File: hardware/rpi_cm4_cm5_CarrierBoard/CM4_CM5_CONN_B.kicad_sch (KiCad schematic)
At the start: 24 parts, among them U17 RPI_CMx_B

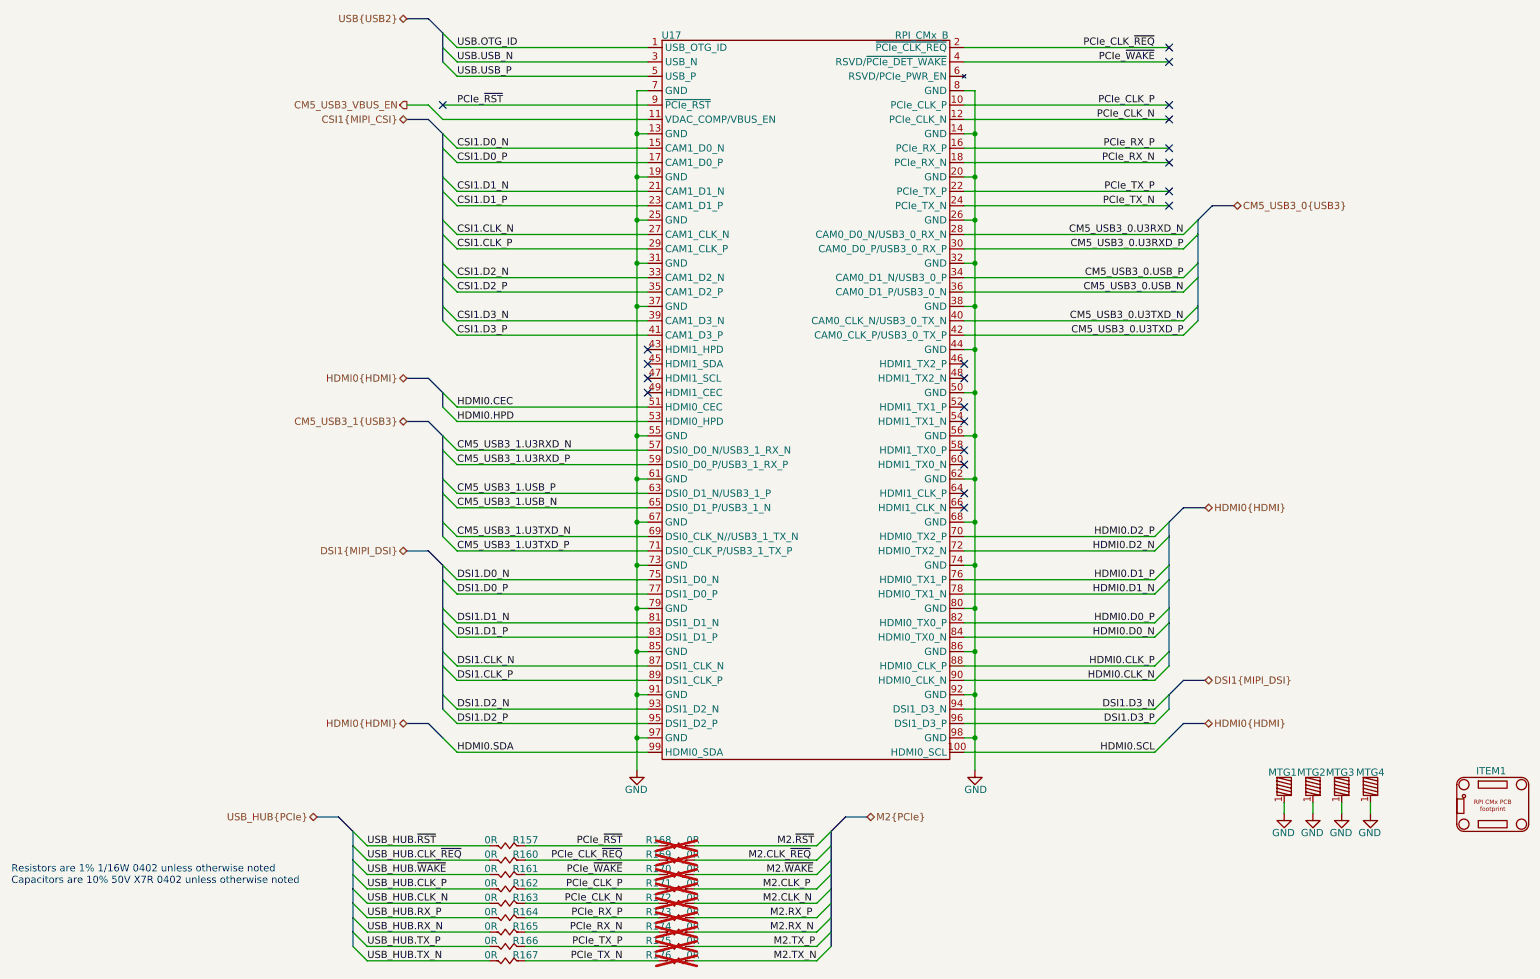
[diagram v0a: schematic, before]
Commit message: Add power-up and power kill sequences Modify schematics to add net classes for DiffPairs
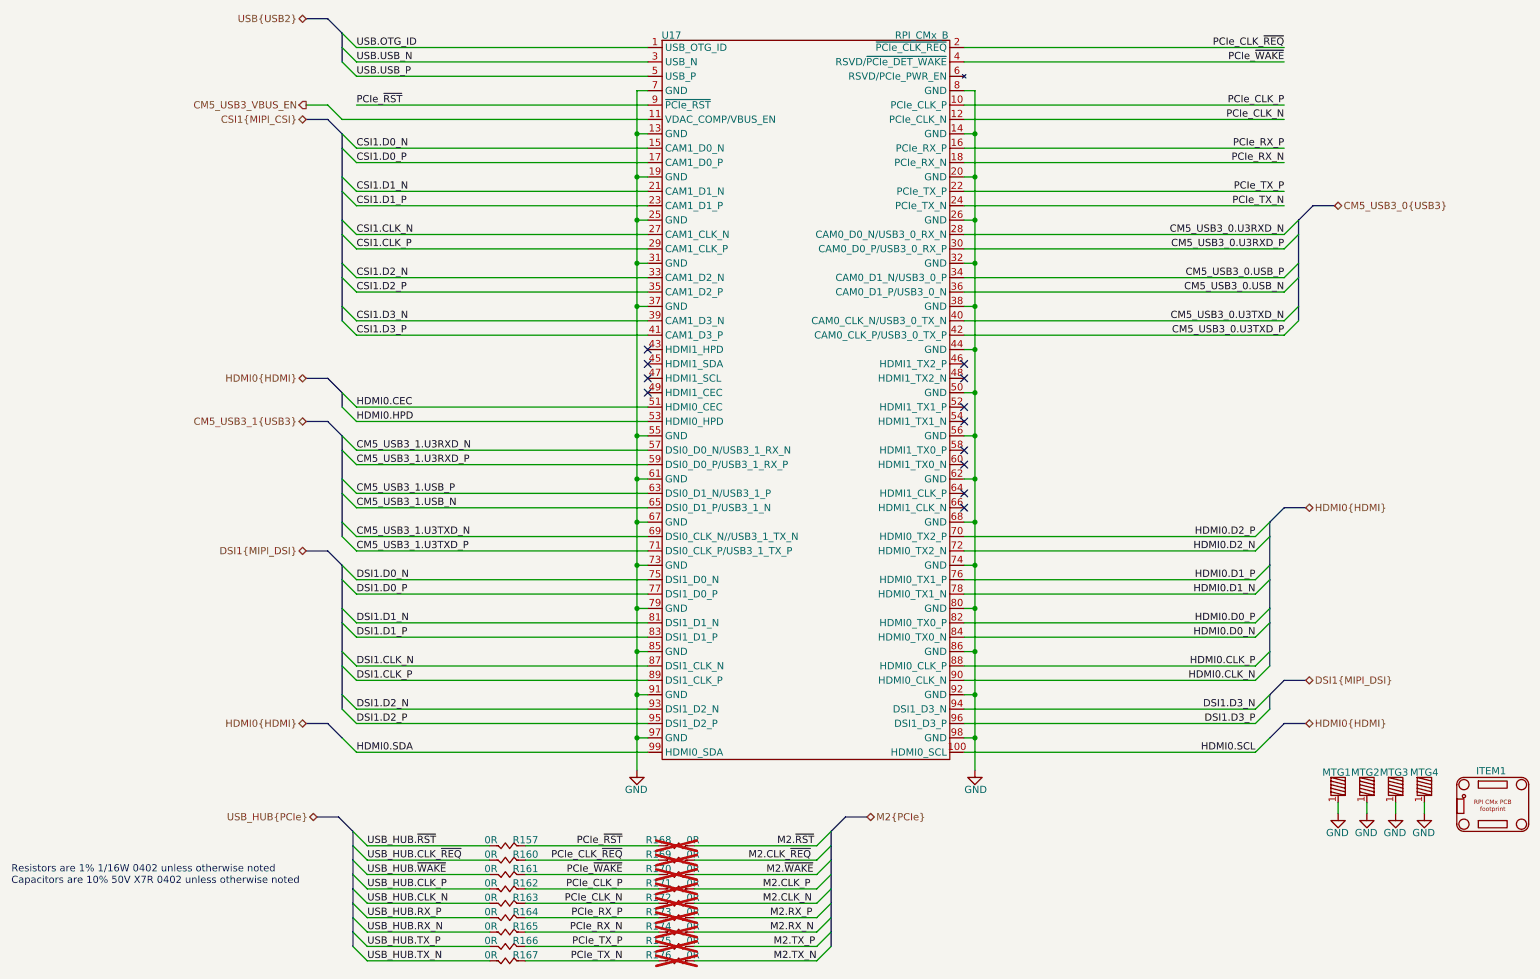
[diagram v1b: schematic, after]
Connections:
- no-connect marks 21 -> 12
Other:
- moved on the sheet: MTG1, MTG2, MTG3, MTG4

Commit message: Significant update to schematics Add codec, Mikrobus, PIC32A Add power table, design notes for pinmux Add datasheets
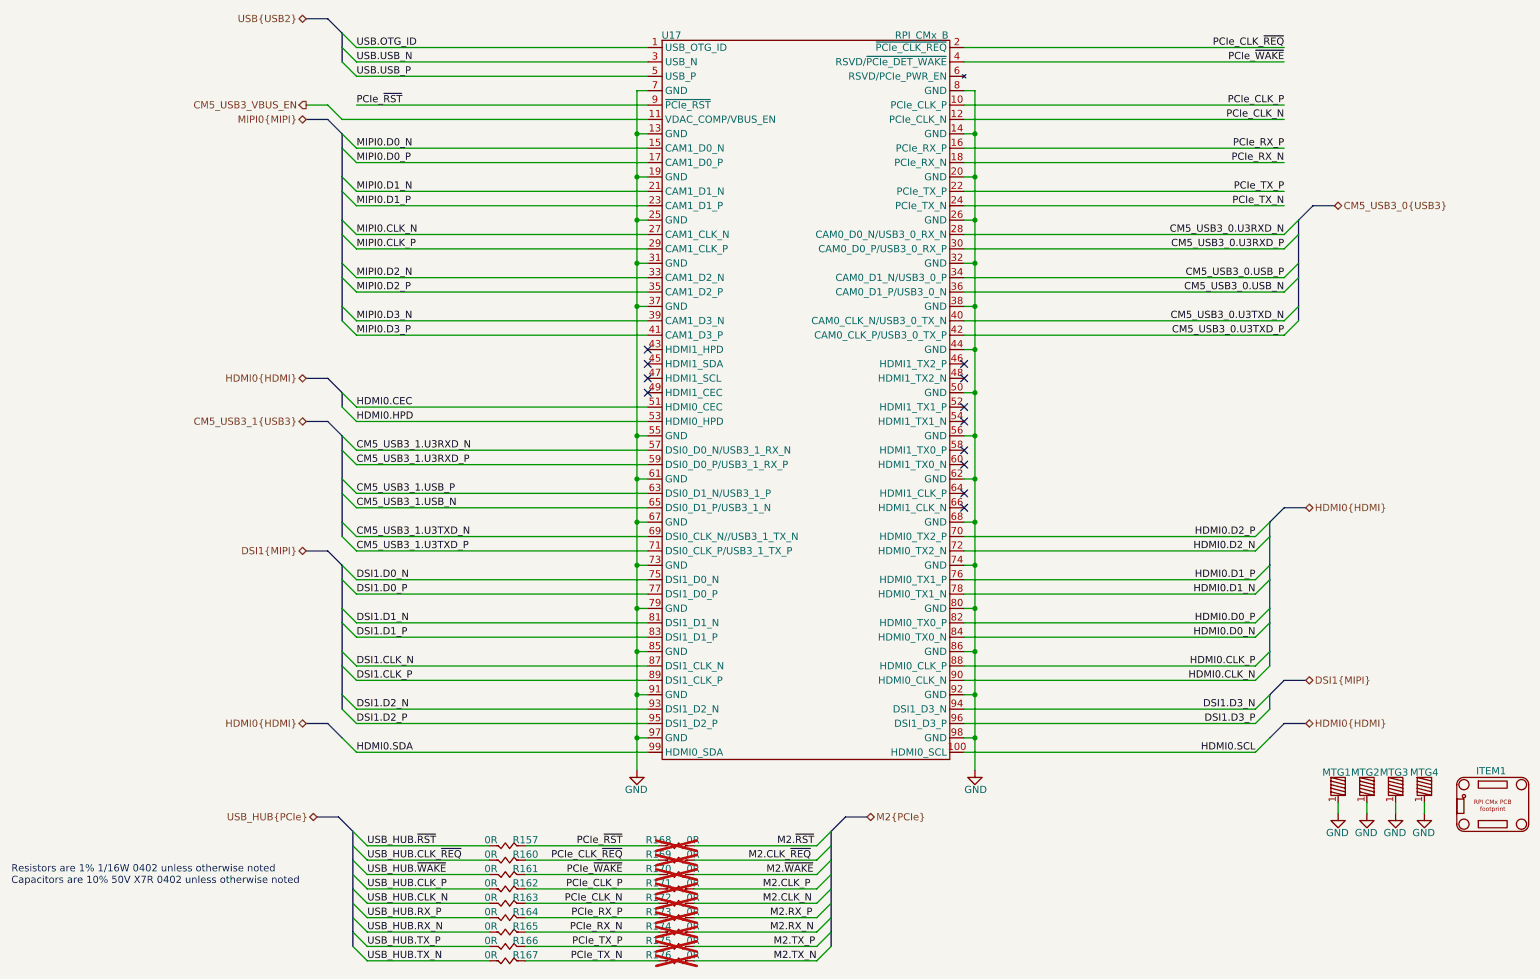
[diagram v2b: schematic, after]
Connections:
- net CSI1.CLK_N renamed MIPI0.CLK_N
- net CSI1.CLK_P renamed MIPI0.CLK_P
- net CSI1.D0_N renamed MIPI0.D0_N
- net CSI1.D0_P renamed MIPI0.D0_P
- net CSI1.D1_N renamed MIPI0.D1_N
- net CSI1.D1_P renamed MIPI0.D1_P
- net CSI1.D2_N renamed MIPI0.D2_N
- net CSI1.D2_P renamed MIPI0.D2_P
- net CSI1.D3_N renamed MIPI0.D3_N
- net CSI1.D3_P renamed MIPI0.D3_P
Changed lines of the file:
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@@
 		(comment 8 "WIP")
 	)
-	(bus_alias "MIPI_CSI"
-		(members "D0_P" "D0_N" "D1_P" "D1_N" "D2_P" "D2_N" "D3_P" "D3_N" "CLK_P"
-			"CLK_N"
-		)
-	)
 	(text "Resistors are 1% 1/16W 0402 unless otherwise noted\nCapacitors are 10% 50V X7R 0402 unless otherwise noted"
 		(exclude_from_sim no)
@@
 		)
 	)
-	(label "CSI1.D2_N"
+	(label "MIPI0.D2_N"
 		(at 73.66 65.405 0)
 		(effects
@@
 		)
 	)
-	(label "CSI1.D3_P"
+	(label "MIPI0.D3_P"
 		(at 73.66 75.565 0)
 		(effects
@@
 		)
 	)
-	(label "CSI1.D0_P"
+	(label "MIPI0.D0_P"
 		(at 73.66 45.085 0)
 		(effects
@@
 		)
 	)
-	(label "CSI1.D2_P"
+	(label "MIPI0.D2_P"
 		(at 73.66 67.945 0)
 		(effects
@@
 		)
 	)
-	(label "CSI1.CLK_N"
+	(label "MIPI0.CLK_N"
 		(at 73.66 57.785 0)
 		(effects
@@
 		)
 	)
-	(label "CSI1.D0_N"
+	(label "MIPI0.D0_N"
 		(at 73.66 42.545 0)
 		(effects
@@
 		)
 	)
-	(label "CSI1.D1_N"
+	(label "MIPI0.D1_N"
 		(at 73.66 50.165 0)
 		(effects
@@
 		)
 	)
-	(label "CSI1.CLK_P"
+	(label "MIPI0.CLK_P"
 		(at 73.66 60.325 0)
 		(effects
@@
 		)
 	)
-	(label "CSI1.D1_P"
+	(label "MIPI0.D1_P"
 		(at 73.66 52.705 0)
 		(effects
@@
 		)
 	)
-	(label "CSI1.D3_N"
+	(label "MIPI0.D3_N"
 		(at 73.66 73.025 0)
 		(effects
@@
 		)
 	)
-	(hierarchical_label "CSI1{MIPI_CSI}"
+	(hierarchical_label "MIPI0{MIPI}"
 		(shape bidirectional)
 		(at 64.77 37.465 180)
@@
 		)
 	)
-	(hierarchical_label "DSI1{MIPI_DSI}"
+	(hierarchical_label "DSI1{MIPI}"
 		(shape bidirectional)
 		(at 241.3 136.525 0)
@@
 		)
 	)
-	(hierarchical_label "DSI1{MIPI_DSI}"
+	(hierarchical_label "DSI1{MIPI}"
 		(shape bidirectional)
 		(at 64.77 113.665 180)

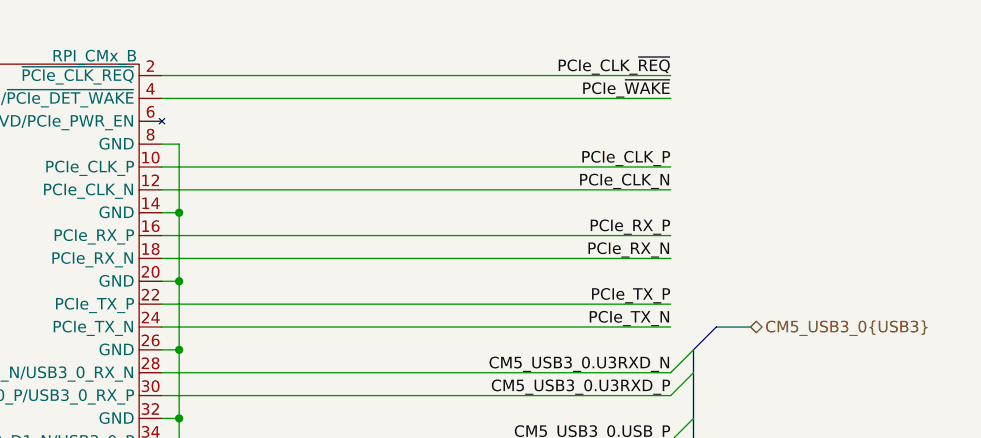
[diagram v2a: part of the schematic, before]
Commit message: Preliminary completion of RPI CMx schematics Cleaned up hierarchical root page
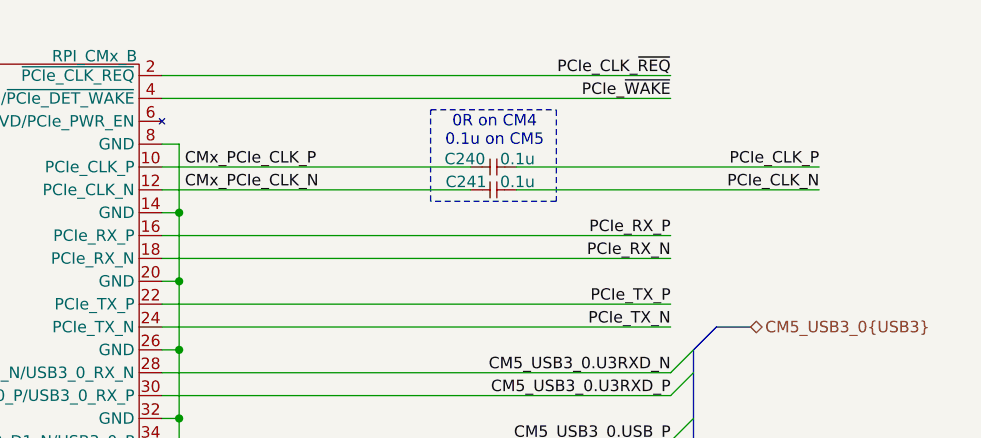
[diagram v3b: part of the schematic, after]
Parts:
- added C240, C241: 0.1u, footprint:CAP_NONPOL_0402, symbol KicadCompDb:Capacitors/CAP_CER_SMT_00001
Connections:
- net PCIe_CLK_N: now also C241.2; no longer U17.12 (PCIe_CLK_N)
- net PCIe_CLK_P: now also C240.2; no longer U17.10 (PCIe_CLK_P)
- new net CMx_PCIe_CLK_N: C241.1, U17.12 (PCIe_CLK_N)
- new net CMx_PCIe_CLK_P: C240.1, U17.10 (PCIe_CLK_P)
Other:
- note added: "0R on CM4 0.1u on CM5"

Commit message: Added power input protection & filter Added dedicated QWIIC connector on RPI CMx I2C6 bus Adjusted power table and PinMux Updated schematics accordingly
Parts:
- U17: now in the parts list
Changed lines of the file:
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@@
 		(unit 1)
 		(exclude_from_sim no)
-		(in_bom no)
+		(in_bom yes)
 		(on_board yes)
 		(dnp no)

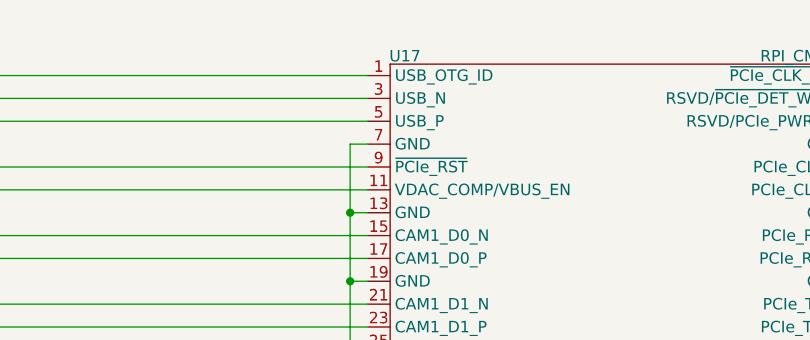
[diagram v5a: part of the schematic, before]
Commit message: Update PCB design rules for outer layers differential pairs Update preliminary component placement Update schematics based on PCB placement & remove duplicata / unnecessary components Update design notes and power table
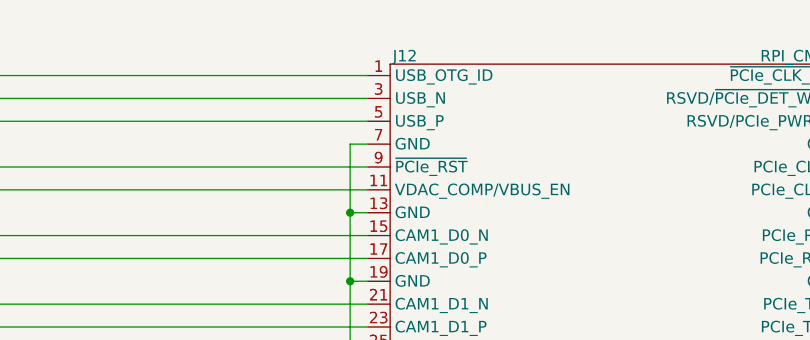
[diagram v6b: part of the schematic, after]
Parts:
- renumbered U17 to J12
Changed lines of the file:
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@@
 		(on_board yes)
 		(dnp no)
-		(property "Reference" "U17"
+		(property "Reference" "J12"
 			(at 129.286 22.606 0)
 			(effects
@@
 			(project ""
 				(path "/7dcdf741-90ca-4333-848c-806f4d64158e/315811e7-ba6e-4f84-a73b-3e30fef30e7f"
-					(reference "U17")
+					(reference "J12")
 					(unit 1)
 				)

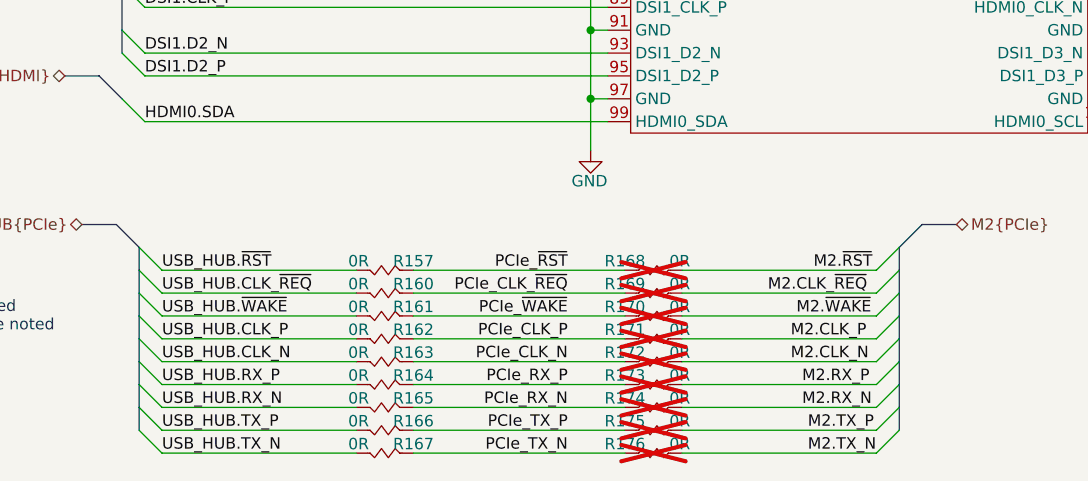
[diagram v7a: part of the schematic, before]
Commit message: Adjust length matching (transmitter vx receiver matching)
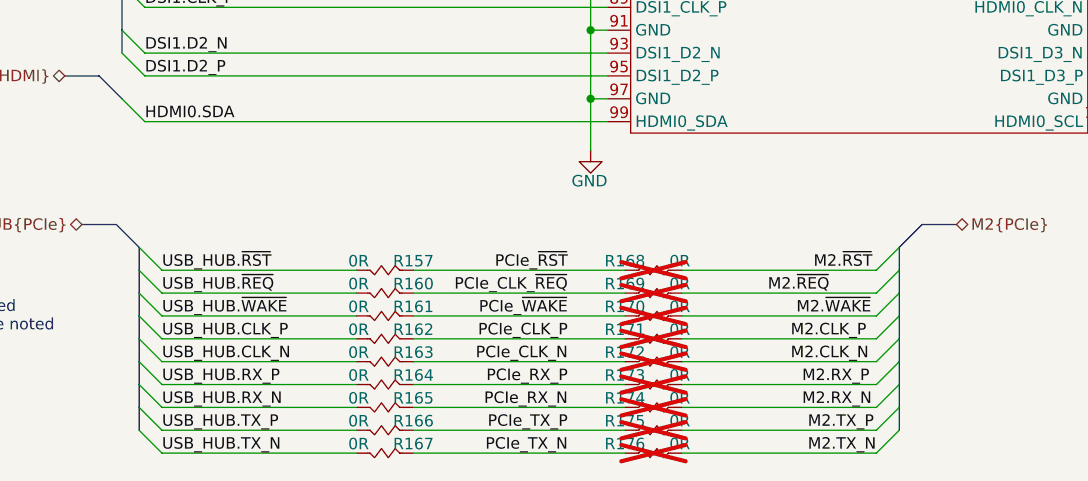
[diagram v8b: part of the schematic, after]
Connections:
- net M2.CLK_~{REQ} renamed M2.~{REQ}
- net USB_HUB.CLK_~{REQ} renamed USB_HUB.~{REQ}
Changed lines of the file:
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@@
 		)
 	)
-	(label "USB_HUB.CLK_~{REQ}"
+	(label "USB_HUB.~{REQ}"
 		(at 75.565 168.275 0)
 		(effects
@@
 		)
 	)
-	(label "M2.CLK_~{REQ}"
+	(label "M2.~{REQ}"
 		(at 142.875 168.275 0)
 		(effects
